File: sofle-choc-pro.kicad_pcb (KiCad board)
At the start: 2 copper layers, 150.5 x 144 mm, 197 parts, among them J1 Connector, USB-TYPE-C-16P, J2 Connector, USB-TYPE-C-16P, J3 OLED 128x32 / nice!view, SW1 BOOT, SW10 F0, SW11 F1, SW12 F2, SW13 F3, SW14 F4, SW15 F5, SW16 F6 Choc/EC11, SW2 RESET, SW20 N0, SW21 N1, SW22 N2, SW23 N3, SW24 N4, SW25 N5, SW30 T0, SW31 T1, SW32 T2, SW33 T3, SW34 T4, SW35 T5, SW40 H0, SW41 H1, SW42 H2, SW43 H3, SW44 H4, SW45 H5, SW50 B0, SW51 B1, SW52 B2, SW53 B3, SW54 B4, SW55 B5, SW60 TH0, SW61 TH1, SW62 TH2, SW63 TH3, SW64 TH4, SW65 TH5 Choc/EC11, U1 RP2040, U2 SRV05-4, U3 W25Q128, U4 SRV05-4, U5 AP2112K-3.3, U6 SN74LV1T34DBVR, X1 ABM8-272-T3

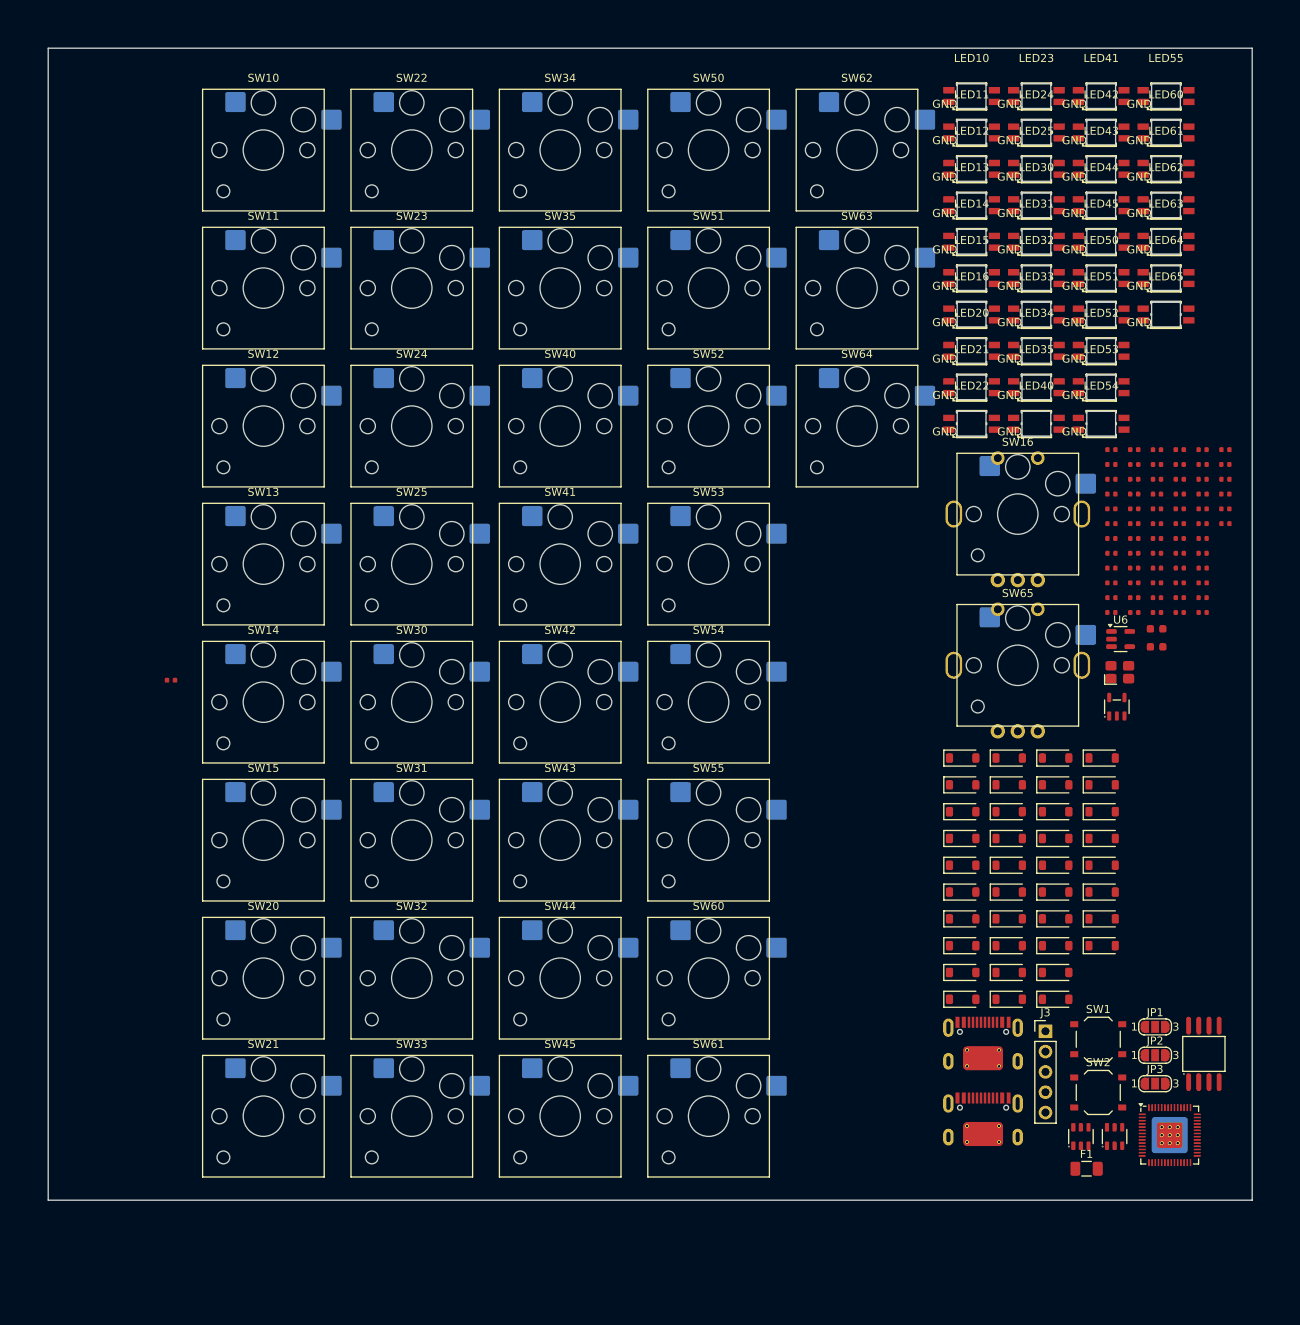
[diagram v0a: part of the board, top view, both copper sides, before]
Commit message: feat(pcb): place the key area from Ergogen and adopt its outline
The board now carries the Ergogen layout, so routing and controller placement can start from the real key positions.

- all 37 switches on their Ergogen points with the per-key LED side; 111 LEDs, caps and diodes snapped to them
- Edge.Cuts replaced by the Ergogen outline; GND pour refilled
- 37 LED footprints updated in place to the 0.55 mm cutout clearance, keeping their schematic links and fields
- C21 removed to match the schematic; DRC schematic parity reports 0 issues
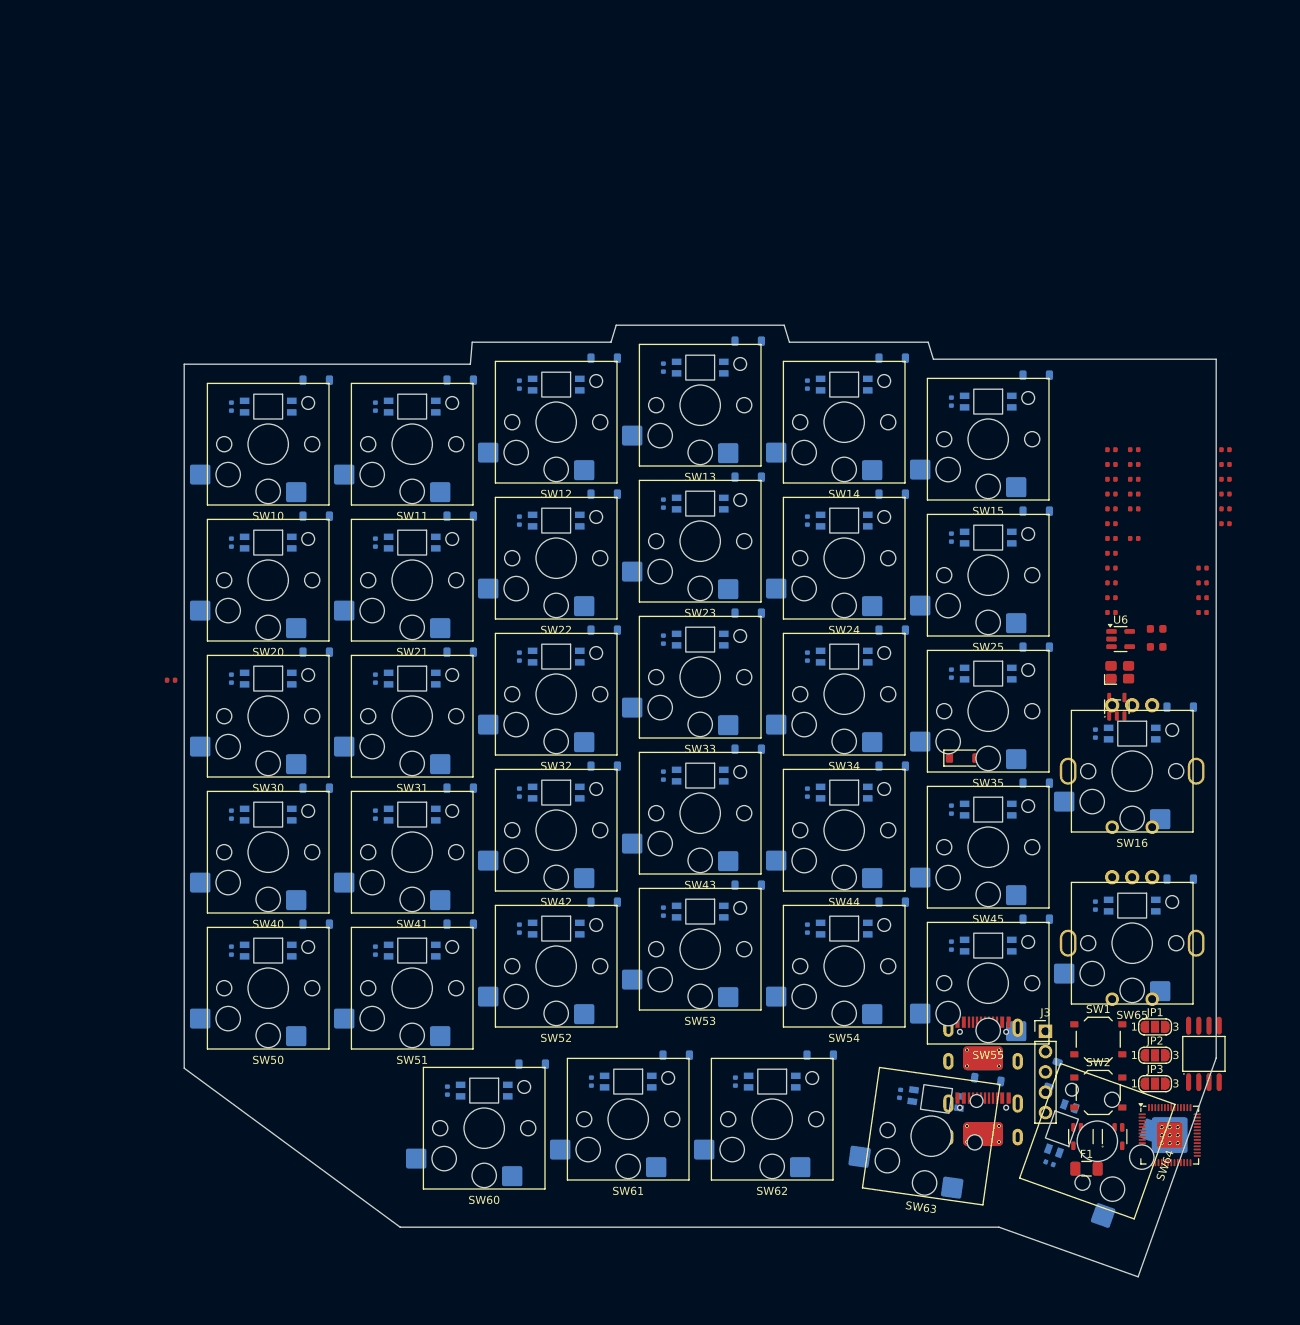
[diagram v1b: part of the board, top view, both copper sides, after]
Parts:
- removed C21: 100nF, PCM_JLCPCB:C_0402
- C110, C111, C112, C113, C114, C115, C116, C120, C121, C122, C123, C124, C125, C130, C131, C132, C133, C134, C135, C140, C141, C142, C143, C144, C145, C150, C151, C152, C153, C154, C155, C160, C161, C162, C163, C164, C165, D10, D11, D12, D13, D14, D15, D16, D20, D21, D22, D23, D24, D25, D30, D31, D32, D33, D34, D35, D40, D41, D42, D43, D44, D45, D50, D51, D52, D53, D54, D55, D60, D61, D62, D63, D64, D65, LED10, LED11, LED12, LED13, LED14, LED15, LED16, LED20, LED21, LED22, LED23, LED24, LED25, LED30, LED31, LED32, LED33, LED34, LED35, LED40, LED41, LED42, LED43, LED44, LED45, LED50, LED51, LED52, LED53, LED54, LED55, LED60, LED61, LED62, LED63, LED64, LED65: moved to B.Cu
- moved LED60 147.0 mm to (87.0, 152.8), turned to 180 degrees
- moved LED50 133.8 mm to (60.0, 135.3), turned to 180 degrees
- moved LED61 132.4 mm to (105.0, 151.7), turned to 180 degrees
- moved C150 127.8 mm to (55.4, 135.3), turned to -90 degrees
- moved C140 125.7 mm to (55.4, 118.3), turned to -90 degrees
- moved LED41 124.4 mm to (78.0, 118.3), turned to 180 degrees
- moved SW62 121.6 mm to (123.0, 156.4), turned to 180 degrees
- moved C160 121.5 mm to (82.4, 152.8), turned to -90 degrees
- moved LED62 120.1 mm to (123.0, 151.7), turned to 180 degrees
- moved SW50 118.3 mm to (60.0, 140.0), turned to 180 degrees
- moved LED51 117.2 mm to (78.0, 135.3), turned to 180 degrees
- moved C130 116.5 mm to (55.4, 101.3), turned to -90 degrees
- moved C120 116.0 mm to (55.4, 84.3), turned to -90 degrees
- moved C110 114.3 mm to (55.4, 67.3), turned to -90 degrees
- moved LED30 112.8 mm to (60.0, 101.3), turned to 180 degrees
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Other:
- board size 150.5 x 144 mm -> 129 x 119 mm

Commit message: feat(pcb): place the controller, connectors and diodes on the keyboard
The Sofle board's own controller parts are placed fresh (not copied from
the module template), with net classes and a fine-pitch clearance rule so
it can be routed on 2 layers at JLCPCB standard limits.

- Controller strip: RP2040 at 45 degrees, host USB-C on the top edge, link
  USB-C on the inner edge above encoder 2, display header on the front
- Easy to reach: BOOT/RESET above the thumbs where the Keebart board has
  them, solder jumpers spaced for an iron below encoder 1
- Routing widths: Power5V 0.5 mm (incl. VBUS), Power3.3V 0.3 mm, USB 0.2 mm;
  0.127 mm clearance allowed only at the RP2040 and USB-C connectors
- Switch diodes stand vertical at each key's top-left; snap_leds.py keeps
  that on re-runs, with a higher spot on the encoder combo keys
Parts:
- C1, C10, C11, C12, C13, C14, C15, C16, C17, C18, C19, C20, C3, C30, C4, C5, C6, C7, C8, C9, D1, F1, J1, J2, JP1, JP2, JP3, R10, R11, R12, R13, R15, R2, R4, R5, R6, R7, R8, SW1, SW2, U1, U2, U3, U4, U5, U6, X1: moved to B.Cu
- moved R15 126.4 mm to (172.2, 124.2), turned to 135 degrees
- moved F1 97.0 mm to (160.9, 65.6), turned to 180 degrees
- moved U4 87.4 mm to (161.5, 71.2)
- moved J1 82.7 mm to (168.7, 66.4)
- moved U1 78.6 mm to (166.0, 80.0), turned to 135 degrees
- moved U3 73.4 mm to (174.8, 74.8)
- moved R4 67.8 mm to (138.7, 145.5), turned to 45 degrees
- moved J2 67.0 mm to (173.2, 93.6), turned to -90 degrees
- moved U2 64.6 mm to (164.5, 94.0)
- moved D1 53.6 mm to (177.3, 67.2), turned to 90 degrees
- moved J3 45.0 mm to (163.9, 100.9), turned to 90 degrees
- moved C30 37.9 mm to (173.4, 121.3), turned to 45 degrees
- moved C18 31.7 mm to (175.1, 65.9), turned to 90 degrees
- moved U6 28.7 mm to (175.8, 123.5), turned to 180 degrees
- moved SW1 28.5 mm to (135.4, 149.3)
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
